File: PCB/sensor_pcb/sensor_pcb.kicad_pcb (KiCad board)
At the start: 2 copper layers, 19 x 18 mm, 6 parts, among them P1 CONN_01X02

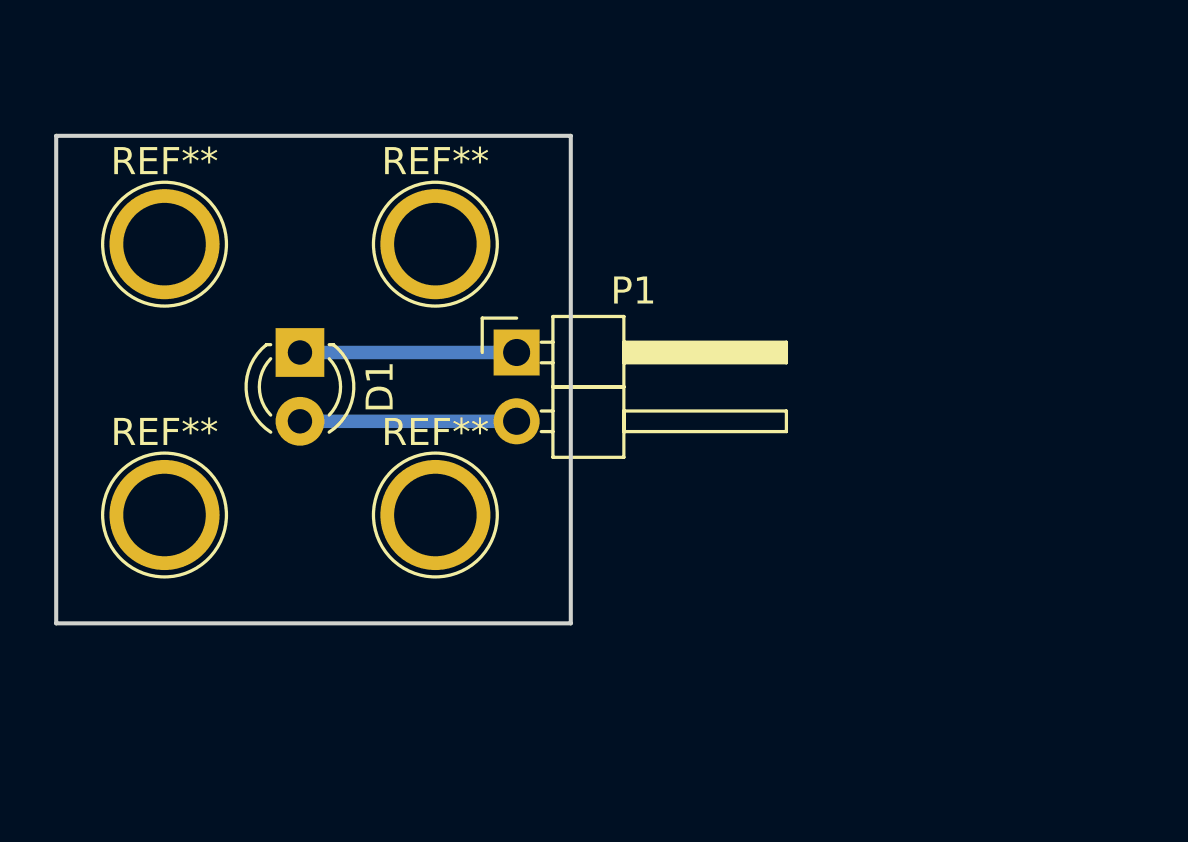
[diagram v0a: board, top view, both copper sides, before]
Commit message: Added supporting PCB layouts
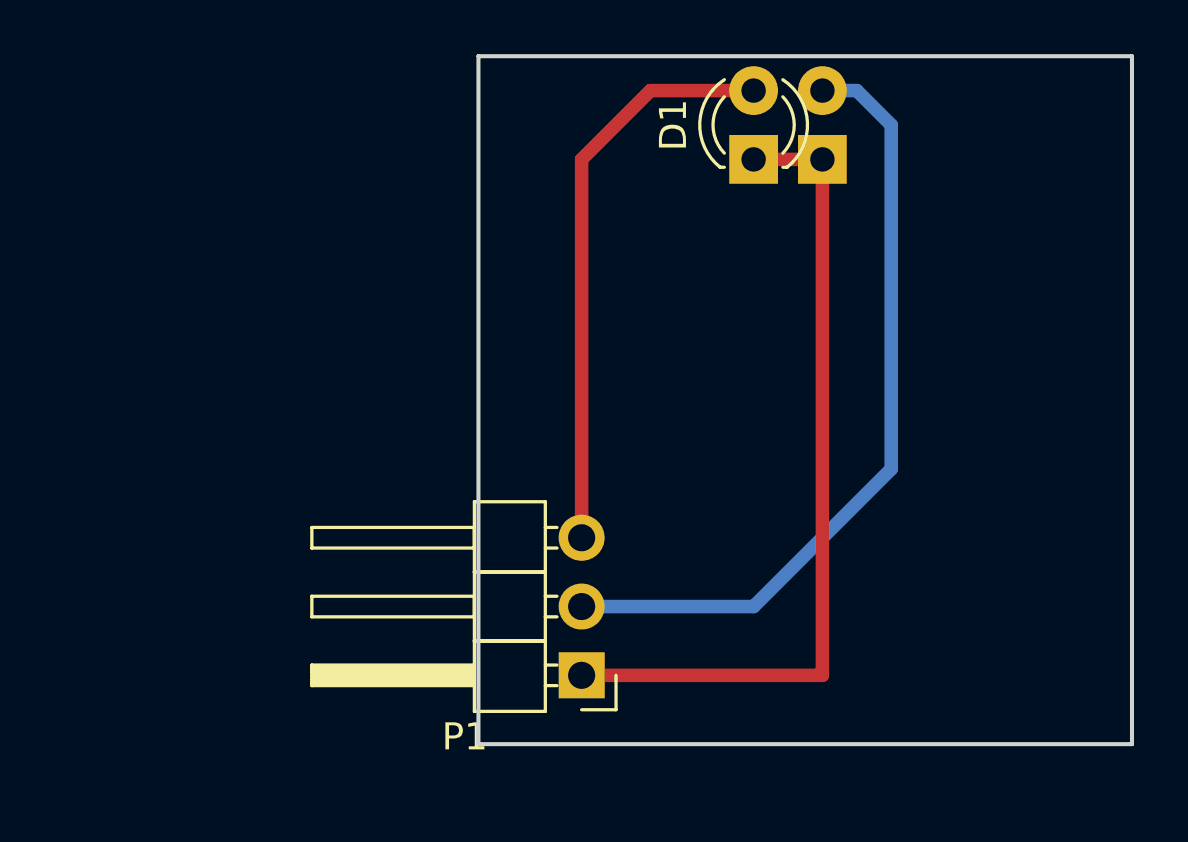
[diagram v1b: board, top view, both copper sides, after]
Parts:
- removed REF** (x4): 1pin, Connect:1pin
- added D2: LED, LEDs:LED_D3.0mm, B.Cu at (161.3, 102.9)
- P1: value CONN_01X02 -> CONN_01X03; footprint Pin_Headers:Pin_Header_Angled_1x02_Pitch2.54mm -> Pin_Headers:Pin_Header_Angled_1x03_Pitch2.54mm
- moved D1 18.2 mm to (158.8, 102.9), turned to 90 degrees
- moved P1 12.2 mm to (152.4, 121.9), turned to 180 degrees
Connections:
- P1 pad 2: Net-(D1-Pad2) -> Net-(D2-Pad2)
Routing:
- net Net-(D2-Pad2): track 0.00 -> 29.3 mm
- net Net-(D1-Pad1): track 8.00 -> 30.5 mm
- net Net-(D1-Pad2): track 8.00 -> 21.4 mm
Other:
- board size 19 x 18 mm -> 24.1 x 25.4 mm

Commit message: minor pcb and BOM adjustments
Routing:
- net Net-(D1-Pad1): track 30.5 -> 35.6 mm, vias 0 -> 1
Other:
- board size 24.1 x 25.4 mm -> 24.4 x 26.9 mm
- net class Default: via_dia 0.6 -> 1.6; via_drill 0.4 -> 0.6
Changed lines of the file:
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@@
     (links 4)
     (no_connects 0)
-    (area 0 0 0 0)
+    (area 141.774999 92.146 193.721715 130.208001)
     (thickness 1.6)
-    (drawings 4)
-    (tracks 11)
+    (drawings 18)
+    (tracks 14)
     (zones 0)
     (modules 3)
@@
     (segment_width 0.2)
     (edge_width 0.15)
-    (via_size 0.6)
-    (via_drill 0.4)
+    (via_size 1.6)
+    (via_drill 0.6)
     (via_min_size 0.4)
     (via_min_drill 0.3)
@@
     (pad_to_mask_clearance 0.2)
     (aux_axis_origin 0 0)
-    (visible_elements FFFFFF7F)
+    (visible_elements 7FFFFFFF)
     (pcbplotparams
-      (layerselection 0x00030_80000001)
+      (layerselection 0x01000_80000001)
       (usegerberextensions false)
       (excludeedgelayer true)
@@
       (outputformat 1)
       (mirror false)
-      (drillshape 1)
+      (drillshape 0)
       (scaleselection 1)
-      (outputdirectory ""))
+      (outputdirectory Gerbers/))
   )
   (net 0 "")
@@
     (clearance 0.2)
     (trace_width 0.5)
-    (via_dia 0.6)
-    (via_drill 0.4)
+    (via_dia 1.6)
+    (via_drill 0.6)
     (uvia_dia 0.3)
     (uvia_drill 0.1)
@@
     )
   )
-  (gr_line (start 148.59 124.46) (end 148.59 99.06) (angle 90) (layer Edge.Cuts) (width 0.15))
-  (gr_line (start 172.72 124.46) (end 148.59 124.46) (angle 90) (layer Edge.Cuts) (width 0.15))
-  (gr_line (start 172.72 99.06) (end 172.72 124.46) (angle 90) (layer Edge.Cuts) (width 0.15))
-  (gr_line (start 148.59 99.06) (end 172.72 99.06) (angle 90) (layer Edge.Cuts) (width 0.15))
-  (segment (start 158.75 102.87) (end 161.29 102.87) (width 0.5) (layer F.Cu) (net 1) (status C00000))
+  (gr_line (start 172.72 103.124) (end 172.72 124.46) (angle 90) (layer Edge.Cuts) (width 0.15))
+  (gr_line (start 148.336 103.124) (end 148.336 124.46) (angle 90) (layer Edge.Cuts) (width 0.15))
+  (gr_line (start 168.656 99.06) (end 152.4 99.06) (angle 90) (layer Edge.Cuts) (width 0.15))
+  (gr_arc (start 168.656 103.124) (end 168.656 99.06) (angle 90) (layer Edge.Cuts) (width 0.15))
+  (gr_arc (start 152.4 103.124) (end 148.336 103.124) (angle 90) (layer Edge.Cuts) (width 0.15))
+  (dimension 24.384 (width 0.3) (layer F.Fab)
+    (gr_text "24.384 mm" (at 160.528 93.646) (layer F.Fab)
+      (effects (font (size 1.5 1.5) (thickness 0.3)))
+    )
+    (feature1 (pts (xy 172.72 99.06) (xy 172.72 92.296)))
+    (feature2 (pts (xy 148.336 99.06) (xy 148.336 92.296)))
+    (crossbar (pts (xy 148.336 94.996) (xy 172.72 94.996)))
+    (arrow1a (pts (xy 172.72 94.996) (xy 171.593496 95.582421)))
+    (arrow1b (pts (xy 172.72 94.996) (xy 171.593496 94.409579)))
+    (arrow2a (pts (xy 148.336 94.996) (xy 149.462504 95.582421)))
+    (arrow2b (pts (xy 148.336 94.996) (xy 149.462504 94.409579)))
+  )
+  (dimension 3.048 (width 0.3) (layer F.Fab)
+    (gr_text "3.048 mm" (at 187.786 124.46 270) (layer F.Fab)
+      (effects (font (size 1.5 1.5) (thickness 0.3)))
+    )
+    (feature1 (pts (xy 162.56 125.984) (xy 189.136 125.984)))
+    (feature2 (pts (xy 162.56 122.936) (xy 189.136 122.936)))
+    (crossbar (pts (xy 186.436 122.936) (xy 186.436 125.984)))
+    (arrow1a (pts (xy 186.436 125.984) (xy 185.849579 124.857496)))
+    (arrow1b (pts (xy 186.436 125.984) (xy 187.022421 124.857496)))
+    (arrow2a (pts (xy 186.436 122.936) (xy 185.849579 124.062504)))
+    (arrow2b (pts (xy 186.436 122.936) (xy 187.022421 124.062504)))
+  )
+  (gr_line (start 172.72 125.984) (end 172.72 124.46) (angle 90) (layer Edge.Cuts) (width 0.15))
+  (gr_line (start 162.56 125.984) (end 172.72 125.984) (angle 90) (layer Edge.Cuts) (width 0.15))
+  (gr_line (start 162.56 124.46) (end 162.56 125.984) (angle 90) (layer Edge.Cuts) (width 0.15))
+  (gr_line (start 158.496 125.984) (end 158.496 124.46) (angle 90) (layer Edge.Cuts) (width 0.15))
+  (gr_line (start 148.336 125.984) (end 158.496 125.984) (angle 90) (layer Edge.Cuts) (width 0.15))
+  (gr_line (start 148.336 124.46) (end 148.336 125.984) (angle 90) (layer Edge.Cuts) (width 0.15))
+  (dimension 23.876 (width 0.3) (layer F.Fab)
+    (gr_text "23.876 mm" (at 181.69 110.998 90) (layer F.Fab)
+      (effects (font (size 1.5 1.5) (thickness 0.3)))
+    )
+    (feature1 (pts (xy 172.72 99.06) (xy 183.04 99.06)))
+    (feature2 (pts (xy 172.72 122.936) (xy 183.04 122.936)))
+    (crossbar (pts (xy 180.34 122.936) (xy 180.34 99.06)))
+    (arrow1a (pts (xy 180.34 99.06) (xy 180.926421 100.186504)))
+    (arrow1b (pts (xy 180.34 99.06) (xy 179.753579 100.186504)))
+    (arrow2a (pts (xy 180.34 122.936) (xy 180.926421 121.809496)))
+    (arrow2b (pts (xy 180.34 122.936) (xy 179.753579 121.809496)))
+  )
+  (dimension 4.064 (width 0.3) (layer F.Fab)
+    (gr_text "4.064 mm" (at 160.528 128.858) (layer F.Fab)
+      (effects (font (size 1.5 1.5) (thickness 0.3)))
+    )
+    (feature1 (pts (xy 162.56 123.952) (xy 162.56 130.208)))
+    (feature2 (pts (xy 158.496 123.952) (xy 158.496 130.208)))
+    (crossbar (pts (xy 158.496 127.508) (xy 162.56 127.508)))
+    (arrow1a (pts (xy 162.56 127.508) (xy 161.433496 128.094421)))
+    (arrow1b (pts (xy 162.56 127.508) (xy 161.433496 126.921579)))
+    (arrow2a (pts (xy 158.496 127.508) (xy 159.622504 128.094421)))
+    (arrow2b (pts (xy 158.496 127.508) (xy 159.622504 126.921579)))
+  )
+  (gr_line (start 162.56 122.936) (end 162.56 124.46) (angle 90) (layer Edge.Cuts) (width 0.15))
+  (gr_line (start 158.496 122.936) (end 162.56 122.936) (angle 90) (layer Edge.Cuts) (width 0.15))
+  (gr_line (start 158.496 124.46) (end 158.496 122.936) (angle 90) (layer Edge.Cuts) (width 0.15))
   (segment (start 161.29 121.92) (end 152.4 121.92) (width 0.5) (layer F.Cu) (net 1))
   (segment (start 161.29 102.87) (end 161.29 121.92) (width 0.5) (layer F.Cu) (net 1))
-  (segment (start 152.4 116.84) (end 152.4 102.87) (width 0.5) (layer F.Cu) (net 2) (status 400000))
-  (segment (start 154.94 100.33) (end 158.75 100.33) (width 0.5) (layer F.Cu) (net 2) (status 800000))
+  (segment (start 158.75 105.41) (end 161.29 105.41) (width 0.5) (layer F.Cu) (net 1))
+  (segment (start 158.75 105.41) (end 158.75 102.87) (width 0.5) (layer F.Cu) (net 1))
+  (via (at 161.29 105.41) (size 1.6) (drill 0.6) (layers F.Cu B.Cu) (net 1))
+  (segment (start 161.29 102.87) (end 161.29 105.41) (width 0.5) (layer B.Cu) (net 1))
+  (segment (start 152.4 116.84) (end 152.4 102.87) (width 0.5) (layer F.Cu) (net 2))
+  (segment (start 154.94 100.33) (end 158.75 100.33) (width 0.5) (layer F.Cu) (net 2))
   (segment (start 152.4 102.87) (end 154.94 100.33) (width 0.5) (layer F.Cu) (net 2))
-  (segment (start 152.4 119.38) (end 158.75 119.38) (width 0.5) (layer B.Cu) (net 3) (status 400000))
-  (segment (start 162.56 100.33) (end 161.29 100.33) (width 0.5) (layer B.Cu) (net 3) (status 800000))
+  (segment (start 152.4 119.38) (end 158.75 119.38) (width 0.5) (layer B.Cu) (net 3))
+  (segment (start 162.56 100.33) (end 161.29 100.33) (width 0.5) (layer B.Cu) (net 3))
   (segment (start 163.83 101.6) (end 162.56 100.33) (width 0.5) (layer B.Cu) (net 3))
   (segment (start 163.83 114.3) (end 163.83 101.6) (width 0.5) (layer B.Cu) (net 3))

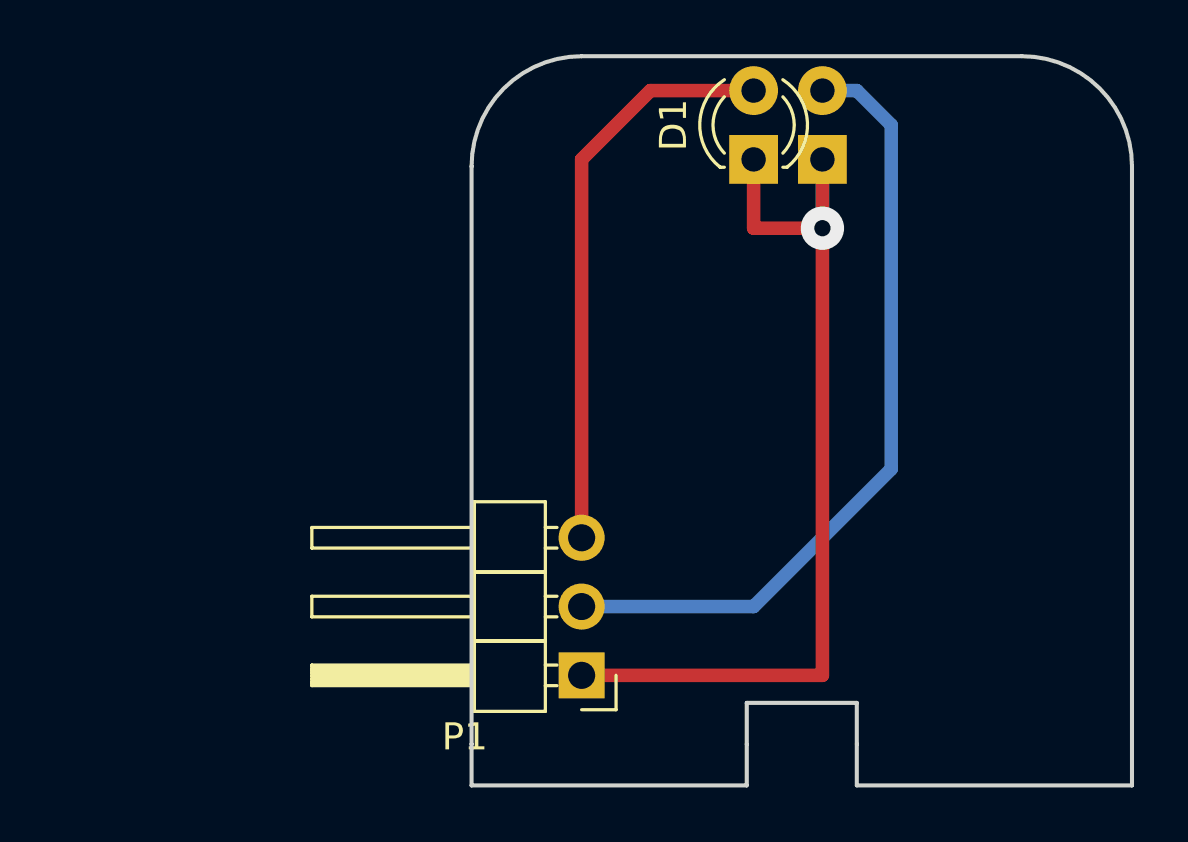
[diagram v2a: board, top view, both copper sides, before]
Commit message: Small pcb adjustments
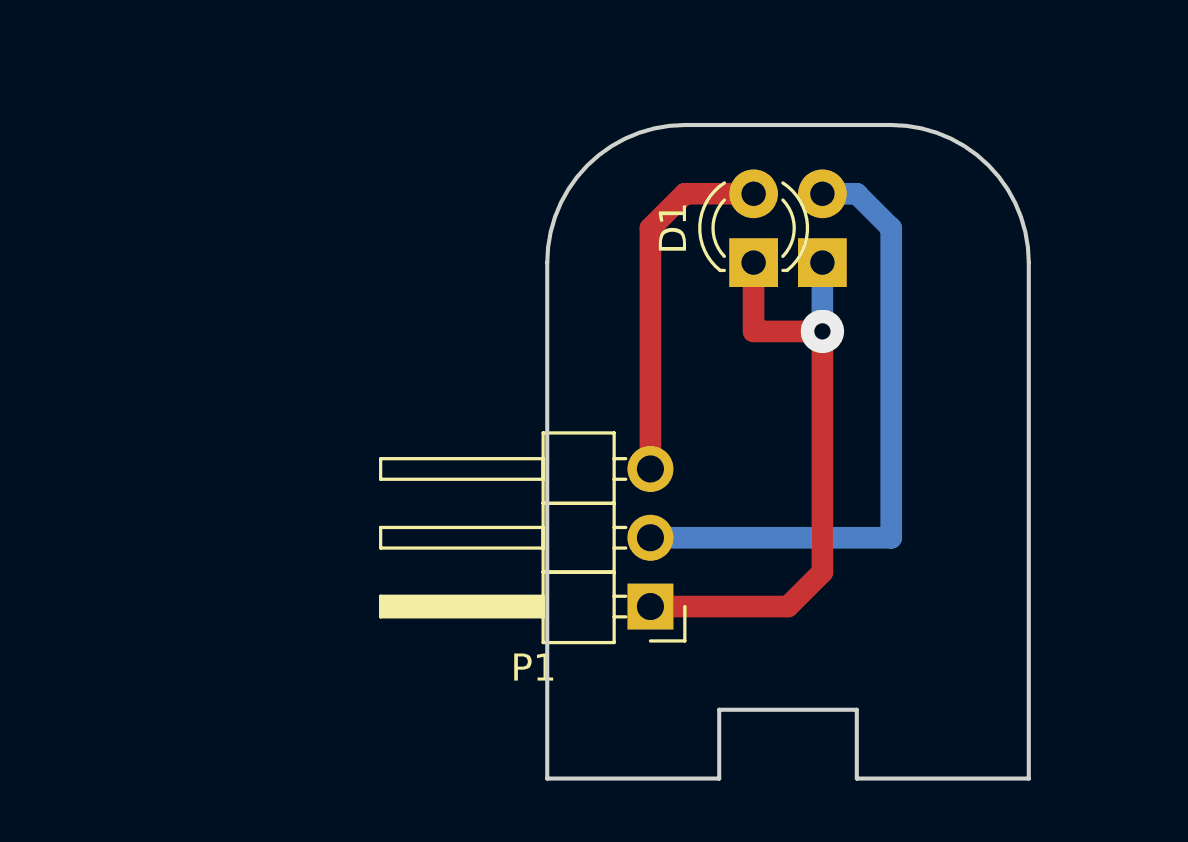
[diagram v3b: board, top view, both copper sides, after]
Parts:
- moved D1 3.81 mm to (158.8, 106.7)
- moved D2 3.81 mm to (161.3, 106.7)
- moved P1 3.59 mm to (154.9, 119.4)
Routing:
- net Net-(D1-Pad1): track 35.6 -> 23.4 mm
- net Net-(D1-Pad2): track 21.4 -> 13.2 mm
- net Net-(D2-Pad2): track 29.3 -> 23.4 mm
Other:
- board size 24.4 x 26.9 mm -> 17.8 x 24.1 mm
- net class Default: trace_width 0.5 -> 0.8

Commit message: Updated sensor pcb to use nte3037 part
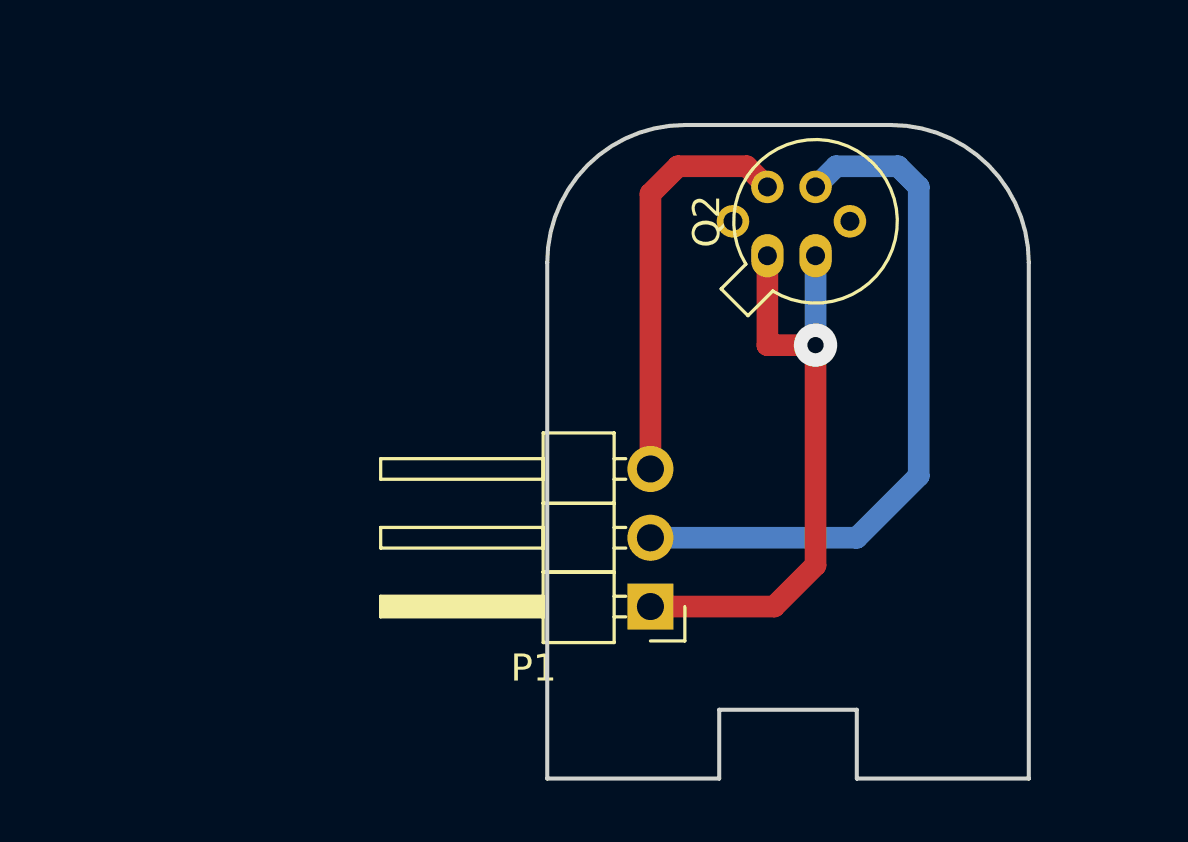
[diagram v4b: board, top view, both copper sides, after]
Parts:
- removed D1, D2: LED, LEDs:LED_D3.0mm
- added Q1: BUT11A, TO_SOT_Packages_THT:TO-18-3_Lens, B.Cu at (159.3, 106.4)
- added Q2: BUT11A, TO_SOT_Packages_THT:TO-18-3_Lens, F.Cu at (161.0, 106.4)
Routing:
- net Net-(P1-Pad2): track 23.4 -> 26.0 mm
- net Net-(P1-Pad3): track 13.2 -> 15.2 mm
